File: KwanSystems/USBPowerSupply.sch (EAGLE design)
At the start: 33 parts, among them J001 USBSMD, J004 M10, J301 JST 2mm, Q050 PMOS, Q201 PMOS, U201 5319, U202 4173, U301 73831

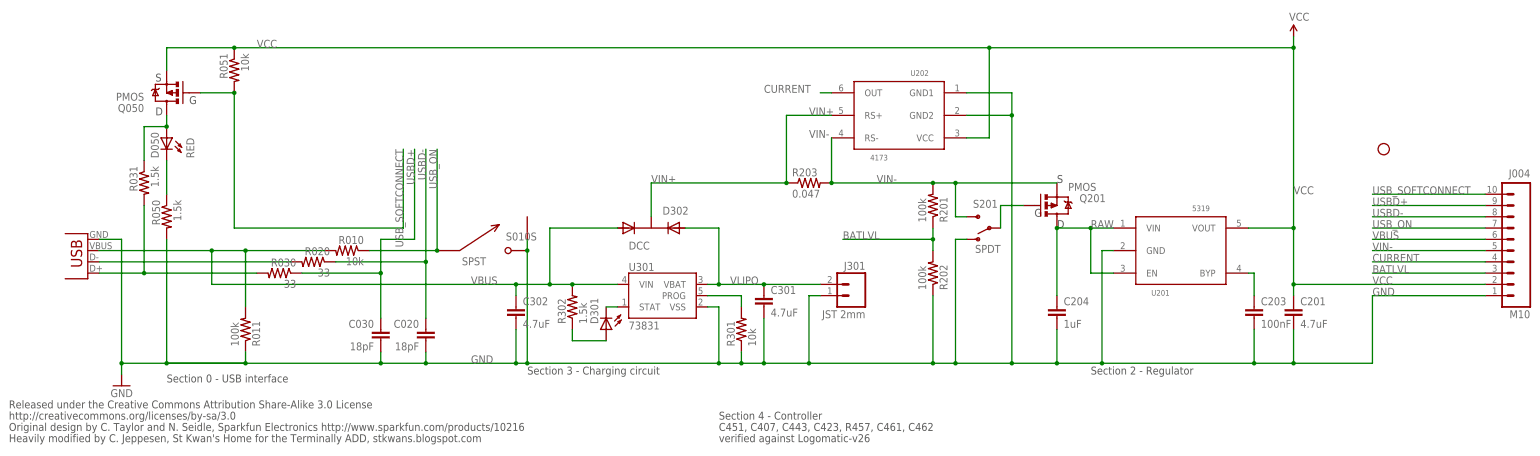
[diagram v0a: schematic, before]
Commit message: Java implementation of Rocketometer filter
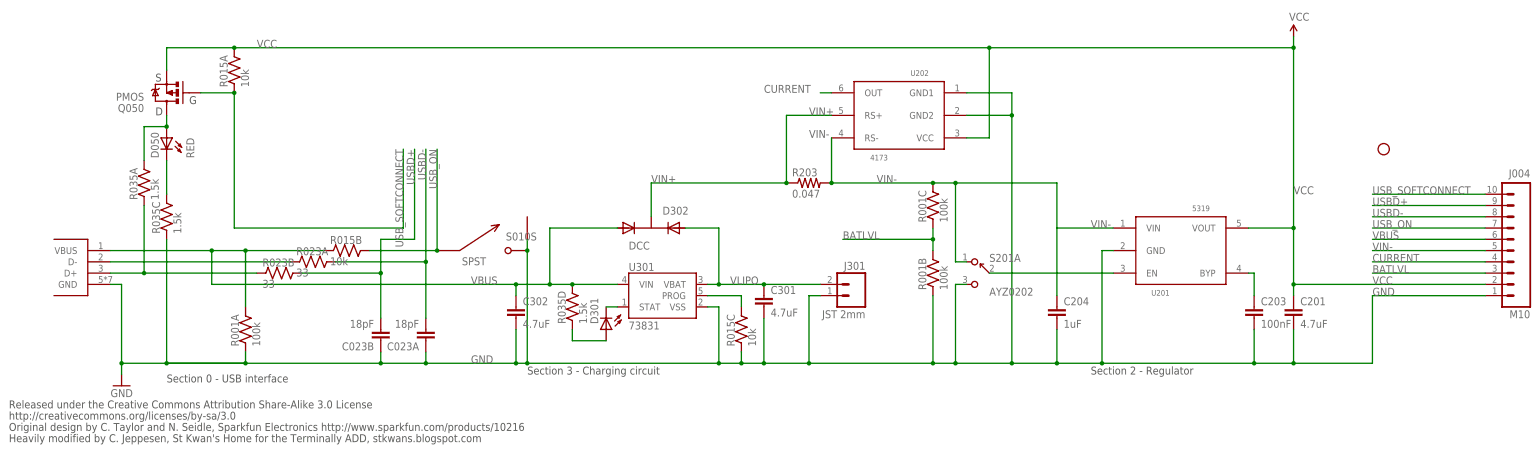
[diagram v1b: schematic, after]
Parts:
- removed C020, C030: 18pF, SparkFun:CAP0402-CAP
- removed Q201: PMOS, SparkFun:MOSFET-PCHANNELSMD
- removed R010, R051, R301: 10k, SparkFun:RESISTOR0402-RES
- removed R011, R201, R202: 100k, SparkFun:RESISTOR0402-RES
- removed R020, R030: 33, SparkFun:RESISTOR0402-RES
- removed R031, R050, R302: 1.5k, SparkFun:RESISTOR0402-RES
- added C023: 18pF, KwanSystems:CKCM25
- added R001: 100k, KwanSystems:RP404
- added R015: 10k, KwanSystems:RP404
- added R023: 33, KwanSystems:RP2EXB24V
- added R035: 1.5k, KwanSystems:RP404
- J001: value USBSMD -> USB_MICROB_JSTGCT; device SparkFun:USBSMD -> KwanSystems:USB_MICROB_JSTGCT
- S201: value SPDT -> AYZ0202; device SparkFun:SWITCH-SPSTSMD -> KwanSystems:AYZ0202
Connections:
- removed net N$10: Q201.G, S201.P
- removed net RAW: C204.1, Q201.D, U201.EN, U201.VIN
- new net N$4: S201A.P$3, U201.EN
- net BATLVL: now also R001B.2, R001C.1; no longer R201.1, R202.2
- net CONN_D+: now also R023B.1, R035A.1; no longer R030.2, R031.2
- net CONN_D-: now also R023A.1; no longer R020.2
- net GND: now also C023A.1, C023B.1, R001A.1, R001B.1, R015C.1, R035C.1, S201A.P$2; no longer C020.2, C030.2, R011.1, R050.2, R202.1, R301.1, S201.O
- net N$1: now also R035D.1; no longer R302.1
- net N$2: now also R015C.2; no longer R301.2
- net N$6: now also R035A.2; no longer R031.1
- net N$7: now also R035C.2; no longer R050.1
- net USBD+: now also C023B.2, R023B.2; no longer C030.1, R030.1
- net USBD-: now also C023A.2, R023A.2; no longer C020.1, R020.1
- net USB_ON: now also R015B.2; no longer R010.1
- net USB_SOFTCONNECT: now also R015A.1; no longer R051.2
- net VBUS: now also R001A.2, R015B.1, R035D.2; no longer R010.2, R011.2, R302.2
- net VCC: now also R015A.2; no longer R051.1
- net VIN-: now also C204.1, R001C.2, S201A.P$1, U201.VIN; no longer Q201.S, R201.2, S201.S
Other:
- note removed: "C451, C407, C443, C423, R457, C461, C462"
- note removed: "Section 4 - Controller"
- note removed: "verified against Logomatic-v26"
